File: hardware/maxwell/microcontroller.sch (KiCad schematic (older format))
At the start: 18 parts, among them U7 STM32F103RETx, Y2 8M, Y3 32.768k

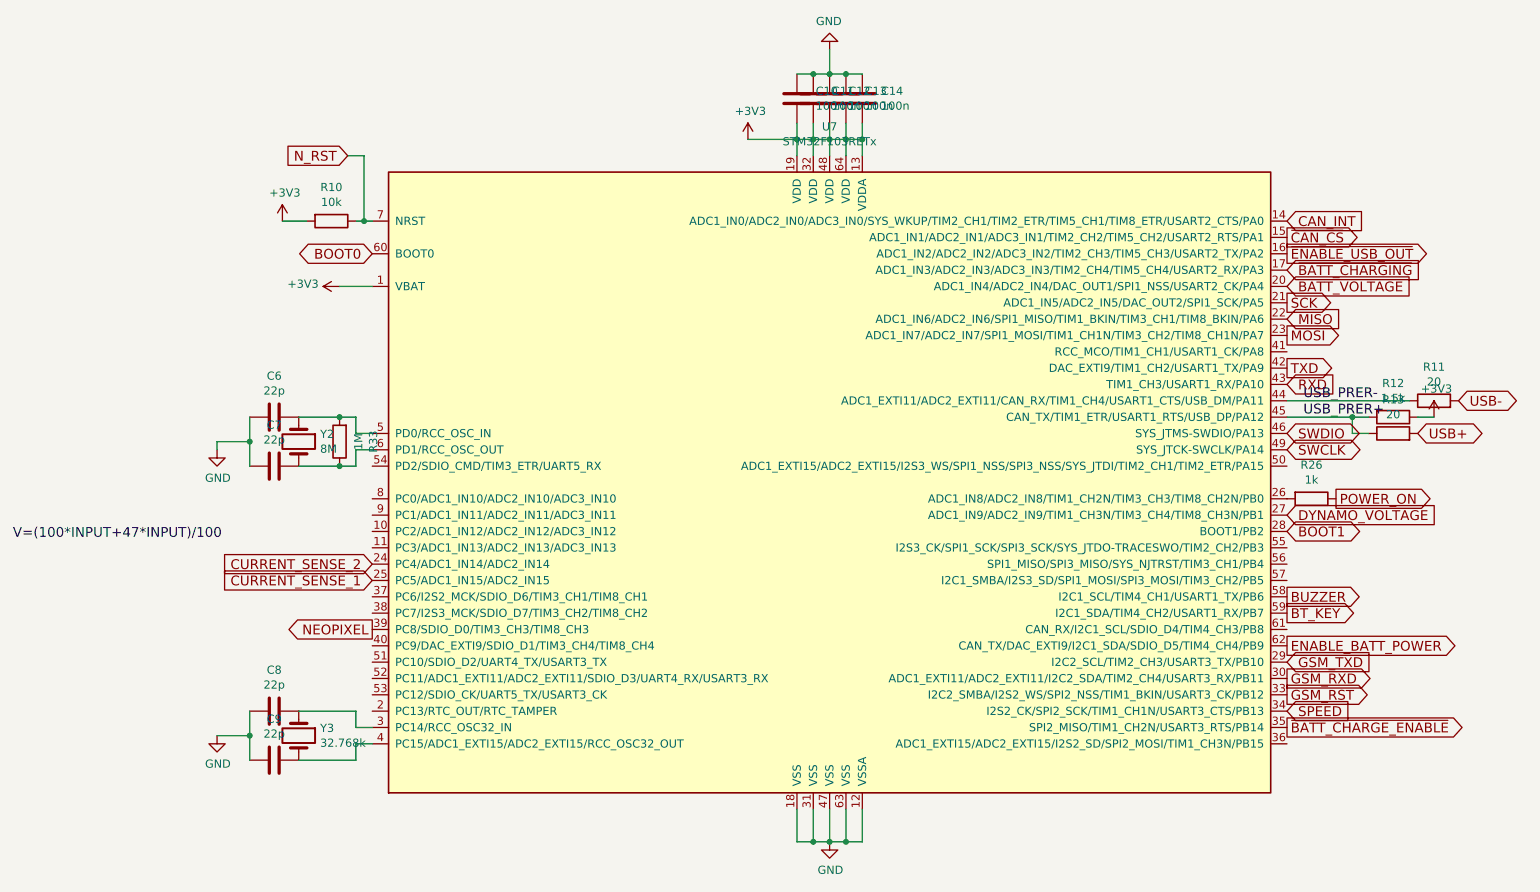
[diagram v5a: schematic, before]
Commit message: Move current measurement to battery side of ldo; obviously.  Also, remove now-redundant second current sense trace.
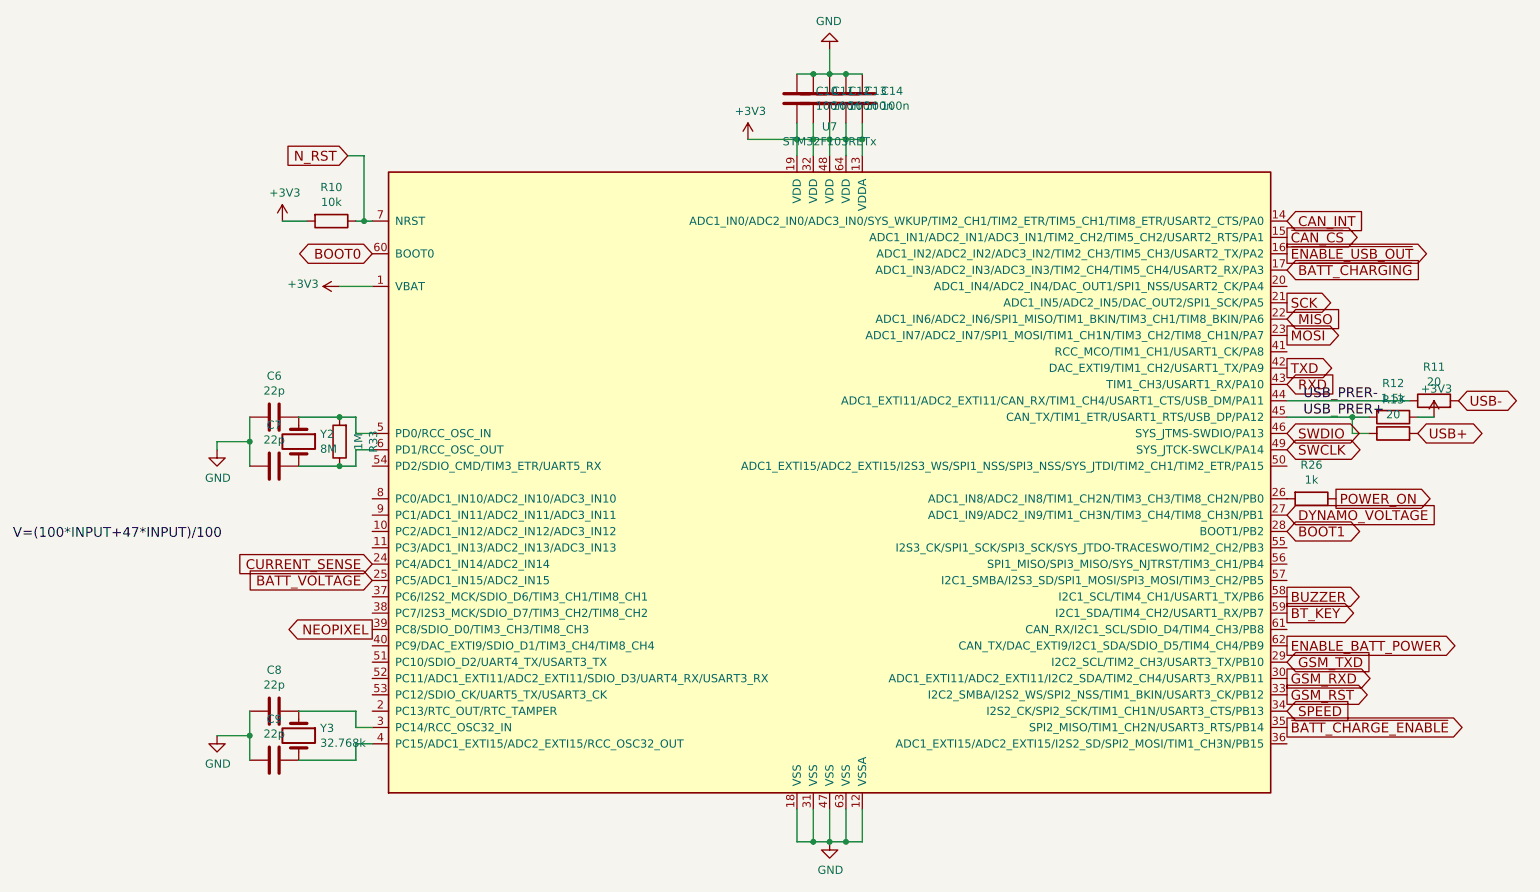
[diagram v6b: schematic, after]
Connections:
- net CURRENT_SENSE_1 is gone; now on net BATT_VOLTAGE: U7.25 (PC5/ADC1_IN15/ADC2_IN15)
- net BATT_VOLTAGE: no longer U7.20 (ADC1_IN4/ADC2_IN4/DAC_OUT1/SPI1_NSS/USART2_CK/PA4)
- net CURRENT_SENSE_2 renamed CURRENT_SENSE
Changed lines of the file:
@@
 $EndComp
 Wire Wire Line
-	2900 2250 2800 2250
+	2800 2250 2900 2250
 Wire Wire Line
 	2500 2250 2350 2250
@@
 Text GLabel 8500 5150 2    60   Output ~ 0
 GSM_RST
+Text GLabel 2900 4350 0    60   Input ~ 0
+CURRENT_SENSE
 Text GLabel 2900 4450 0    60   Input ~ 0
-CURRENT_SENSE_1
-Text GLabel 2900 4350 0    60   Input ~ 0
-CURRENT_SENSE_2
-Text GLabel 8500 2650 2    60   Input ~ 0
 BATT_VOLTAGE
 Text Notes 700  4200 0    60   ~ 0
